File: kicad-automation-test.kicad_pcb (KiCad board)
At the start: 2 copper layers, 20 x 20 mm, 7 parts, among them J1 Input

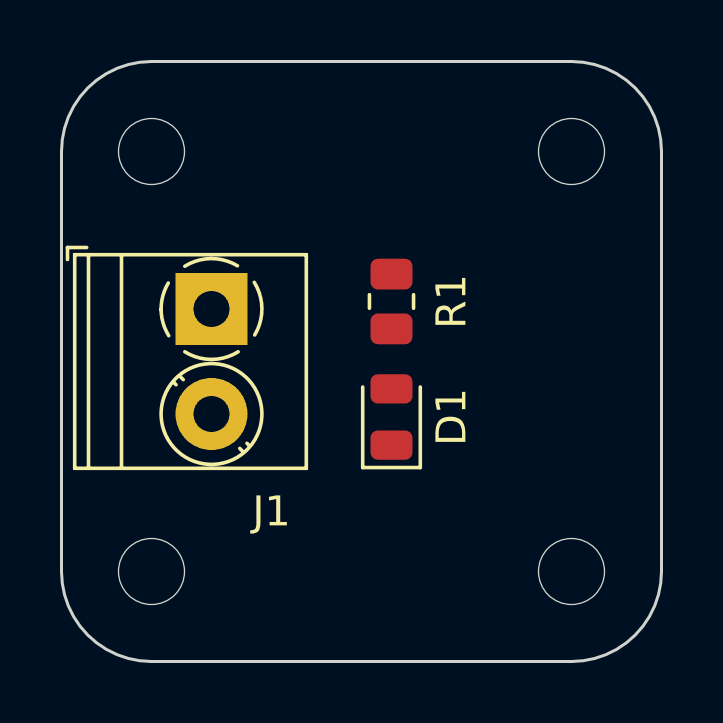
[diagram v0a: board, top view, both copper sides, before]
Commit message: Removed quickstart workflow and added PCB tracking
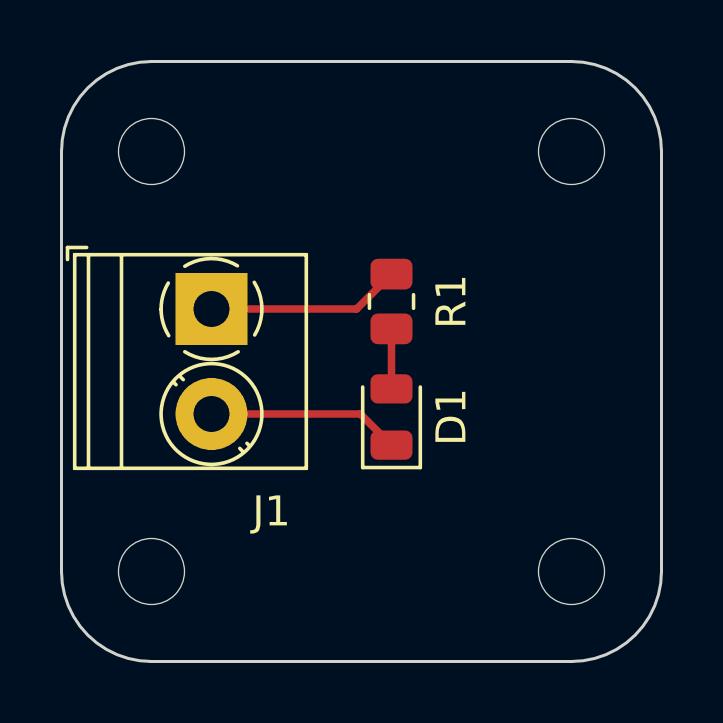
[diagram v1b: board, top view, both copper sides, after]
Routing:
- net Net-(J1-Pad1): track 0.00 -> 6.48 mm
- net Net-(D1-Pad1): track 0.00 -> 6.43 mm
- net Net-(D1-Pad2): track 0.00 -> 2.00 mm
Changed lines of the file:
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@@
     (style (thickness 0.15) (arrow_length 1.27) (text_position_mode 0) (extension_height 0.58642) (extension_offset 0.5) keep_text_aligned)
   )
+  (segment (start 140.9625 91.75) (end 136 91.75) (width 0.25) (layer "F.Cu") (net 1))
+  (segment (start 142 92.7875) (end 140.9625 91.75) (width 0.25) (layer "F.Cu") (net 1))
+  (segment (start 142 88.9125) (end 142 90.9125) (width 0.25) (layer "F.Cu") (net 2))
+  (segment (start 140.8375 88.25) (end 136 88.25) (width 0.25) (layer "F.Cu") (net 3))
+  (segment (start 142 87.0875) (end 140.8375 88.25) (width 0.25) (layer "F.Cu") (net 3))
 )
